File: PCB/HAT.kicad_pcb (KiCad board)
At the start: 2 copper layers, 104 parts, among them J1 Conn_01x02_Pin, J10 Conn_01x24_Socket, J11 Conn_01x24_Pin, J12 Conn_01x02_Pin, J13 Conn_01x02_Pin, J14 Conn_01x02_Pin, J15 Conn_01x02_Pin, J2 Conn_01x02_Pin, J3 Conn_01x01_Pin, J4 Conn_01x02_Pin, J5 Conn_01x10_Pin, J6 MICROXNJ, J7 Conn_01x01_Pin, J8 Conn_01x24_Pin, J9 Conn_01x24_Socket, Q1 AO3401A, Q2 LBSS84LT1G, Q3 LBSS84LT1G, Q4 BSS138, Q5 BSS138, Q6 BSS138, Q7 BSS138, Q8 LM317AG-TN3-R, U1 TP4056, U2 XC6206P, U3 OP07, U4 VL6180, U5 LM317AG, U6 CAT24C256, U7 CH340C, Y1 C252310

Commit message: PCB_Design_1
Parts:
- removed U5: LM317AG, JLC_Misc:TO-252-2_L6.5-W6.1-P4.58-LS10.0-TL
- J11, J8: footprint Connector_PinSocket_2.54mm:PinSocket_1x24_P2.54mm_Vertical -> Connector_PinHeader_2.54mm:PinHeader_1x24_P2.54mm_Vertical
- J12, J13, J14, J15: footprint Connector_PinSocket_2.54mm:PinSocket_1x02_P2.54mm_Vertical -> Connector_PinHeader_2.54mm:PinHeader_1x02_P2.54mm_Vertical
- moved R16 87.1 mm to (180.9, 52.9), turned to 90 degrees
- moved R18 85.6 mm to (180.0, 145.0)
- moved R15 83.6 mm to (177.9, 52.9), turned to 90 degrees
- moved R14 80.2 mm to (175.0, 52.9), turned to 90 degrees
- moved U4 79.0 mm to (203.1, 73.0)
- moved R19 77.7 mm to (190.1, 123.2)
- moved R20 77.7 mm to (190.1, 126.1)
- moved R21 77.7 mm to (190.1, 129.1)
- moved R22 77.7 mm to (190.1, 132.0)
- moved R23 77.7 mm to (190.1, 134.9)
- moved R24 77.7 mm to (190.1, 137.9)
- moved R25 77.7 mm to (190.1, 140.8)
- moved U3 75.8 mm to (172.6, 46.0), turned to 90 degrees
- moved D3 72.7 mm to (182.0, 47.0), turned to -90 degrees
- moved R11 70.8 mm to (158.0, 50.0)
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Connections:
- J8 pad 13: /MicroController_Interfacing/USB 5V -> Net-(J8-Pin_13)
- J9 pad 13: /MicroController_Interfacing/USB 5V -> Net-(J8-Pin_13)

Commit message: sensor layout pcb
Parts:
- moved R51 124.5 mm to (96.9, 110.0), turned to 180 degrees
- moved R50 122.5 mm to (96.6, 95.3), turned to 180 degrees
- moved R49 122.0 mm to (100.4, 113.9), turned to 90 degrees
- moved R48 120.1 mm to (100.1, 99.2), turned to 90 degrees
- moved J15 116.9 mm to (103.2, 104.8), turned to -90 degrees
- moved J14 112.3 mm to (102.8, 90.1), turned to -90 degrees
- moved R47 111.1 mm to (105.8, 114.0), turned to 90 degrees
- moved R45 110.4 mm to (106.7, 109.0), turned to 180 degrees
- moved R46 109.6 mm to (105.5, 99.3), turned to 90 degrees
- moved R44 108.8 mm to (106.4, 94.3), turned to 180 degrees
- moved U6 104.0 mm to (203.1, 121.7)
- moved R31 103.7 mm to (207.1, 79.2)
- moved R32 103.7 mm to (207.1, 82.2)
- moved R33 103.7 mm to (207.1, 85.2)
- moved R34 103.7 mm to (207.1, 88.1)
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
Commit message: Modified PCB
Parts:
- J7: value Conn_01x01_Pin -> GND
- moved J6 117.8 mm to (188.1, 68.8), turned to 90 degrees
- moved C12 101.9 mm to (169.5, 63.7), turned to 180 degrees
- moved U7 93.4 mm to (172.7, 69.1), turned to 90 degrees
- moved C15 79.0 mm to (162.8, 72.2), turned to -90 degrees
- moved J7 78.5 mm to (165.1, 57.3)
- moved U6 71.3 mm to (149.8, 74.3), turned to 90 degrees
- moved C10 65.3 mm to (136.4, 72.4), turned to 90 degrees
- moved C13 64.5 mm to (159.8, 75.7)
- moved C14 62.6 mm to (162.8, 75.6)
- moved R28 61.1 mm to (143.6, 69.5), turned to 90 degrees
- moved R26 59.0 mm to (143.9, 74.0), turned to 90 degrees
- moved R30 57.2 mm to (149.7, 69.3), turned to -90 degrees
- moved R27 56.9 mm to (147.2, 69.4), turned to 90 degrees
- moved C16 55.4 mm to (159.8, 72.2), turned to -90 degrees
- moved R29 52.8 mm to (153.3, 69.3), turned to -90 degrees
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
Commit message: PCB_Design_1
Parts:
- moved R5 59.1 mm to (94.0, 43.1), turned to -90 degrees
- moved R1 48.4 mm to (176.1, 57.0), turned to 180 degrees
- moved C4 46.9 mm to (100.0, 54.3)
- moved R6 46.8 mm to (106.0, 55.0), turned to 90 degrees
- moved C2 45.2 mm to (177.5, 48.0), turned to 180 degrees
- moved J1 43.9 mm to (171.0, 56.0)
- moved Q3 43.6 mm to (161.0, 56.2), turned to -90 degrees
- moved R17 42.6 mm to (165.1, 57.0), turned to 180 degrees
- moved LED1 41.6 mm to (115.2, 45.0), turned to 0 degrees
- moved D1 39.8 mm to (127.0, 52.0), turned to 180 degrees
- moved U2 39.2 mm to (176.0, 52.0), turned to 0 degrees
- moved LED2 38.8 mm to (115.1, 48.0), turned to 180 degrees
- moved Q1 38.8 mm to (127.0, 56.0), turned to 0 degrees
- moved R4 38.7 mm to (108.1, 48.0)
- moved U1 38.7 mm to (100.6, 44.8)
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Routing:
- net /Power Module/V_BAT+: track 0.00 -> 253.0 mm, vias 0 -> 2
- net /MicroController_Interfacing/3V3: track 0.00 -> 220.9 mm
- net /MicroController_Interfacing/A0: track 0.00 -> 123.0 mm, vias 0 -> 1
- net /MicroController_Interfacing/USB 5V: track 0.00 -> 118.3 mm, vias 0 -> 1
- net /MicroController_Interfacing/GPIO 0: track 0.00 -> 104.1 mm, vias 0 -> 1
- net /Sensor Module/Logic Level Shifting/2V8: track 0.00 -> 97.1 mm, vias 0 -> 5
- net /MicroController_Interfacing/GPIO 1: track 0.00 -> 88.6 mm, vias 0 -> 3
- net USART_TX: track 0.00 -> 82.7 mm, vias 0 -> 1
- net USART_RX: track 0.00 -> 80.7 mm, vias 0 -> 1
- net /Power Module/UVLO_3V3: track 0.00 -> 69.8 mm
- net /MicroController_Interfacing/DigitalSensorSDA: track 0.00 -> 69.7 mm
- net /Sensor Module/Logic Level Shifting/A1: track 0.00 -> 65.0 mm, vias 0 -> 1
- net Net-(D1-A): track 0.00 -> 57.0 mm
- net /MicroController_Interfacing/DigitalSensorSCL: track 0.00 -> 56.0 mm
- net /Power Module/CHRG_OUT: track 0.00 -> 48.9 mm
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- added copper zone on F.Cu, net GND

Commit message: DRCs done
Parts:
- J7: value GND -> Conn_01x01_Pin
- moved LED2 0.11 mm to (114.9, 48.0)
- moved Q2 0.10 mm to (141.1, 56.1)
- moved Q3 0.09 mm to (160.9, 56.1)
- moved C15 0.05 mm to (162.8, 72.2)
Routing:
- net GND: track 9.05 -> 213.0 mm, vias 0 -> 12
- net Net-(D1-A): track 57.0 -> 71.3 mm
- net Net-(J4-Pin_2): track 0.00 -> 7.62 mm
- net unconnected-(J6-Shield-Pad6): track 11.9 -> 13.5 mm
- net EEPROMSCL: track 17.2 -> 17.0 mm, vias 1 -> 2
- net /Sensor Module/Logic Level Shifting/2V8: vias 5 -> 4
- net /Power Module/V_BAT+: vias 2 -> 3
- added copper zone on B.Cu, net GND
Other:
- board outline added: 99.4 x 99 mm

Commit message: updated Gerbers!
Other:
- board text added: "EEE3088F GROUP 3"
- board text added: "Michael Awe AWXMIC001 Simon Carthew CRTSIM008 Adrian McIntosh MCNADR001"

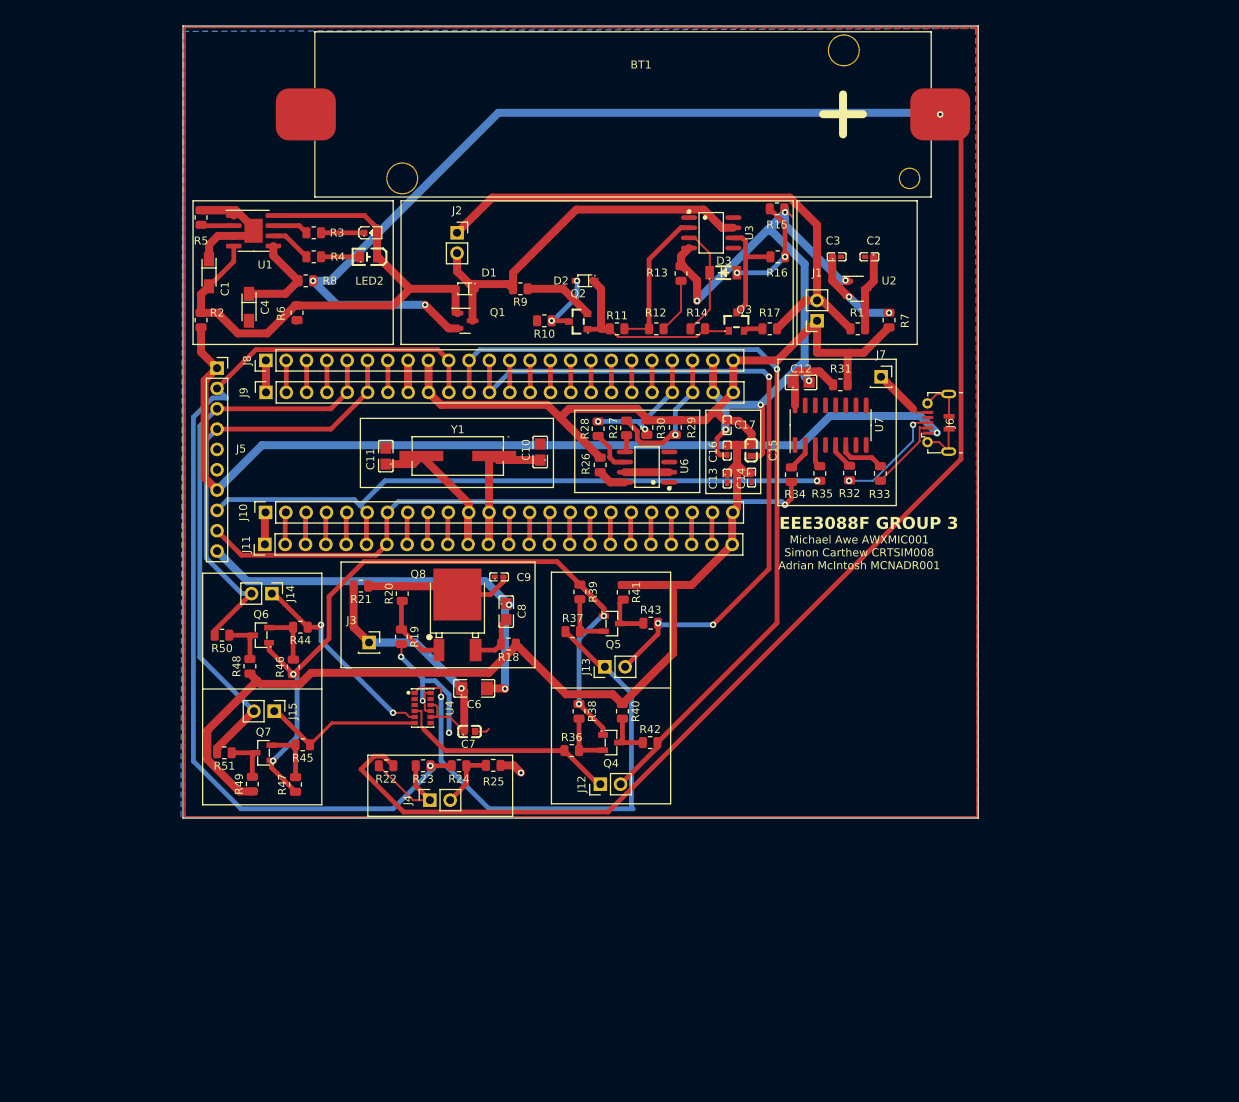
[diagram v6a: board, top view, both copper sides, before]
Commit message: Fixed via issues on PCB
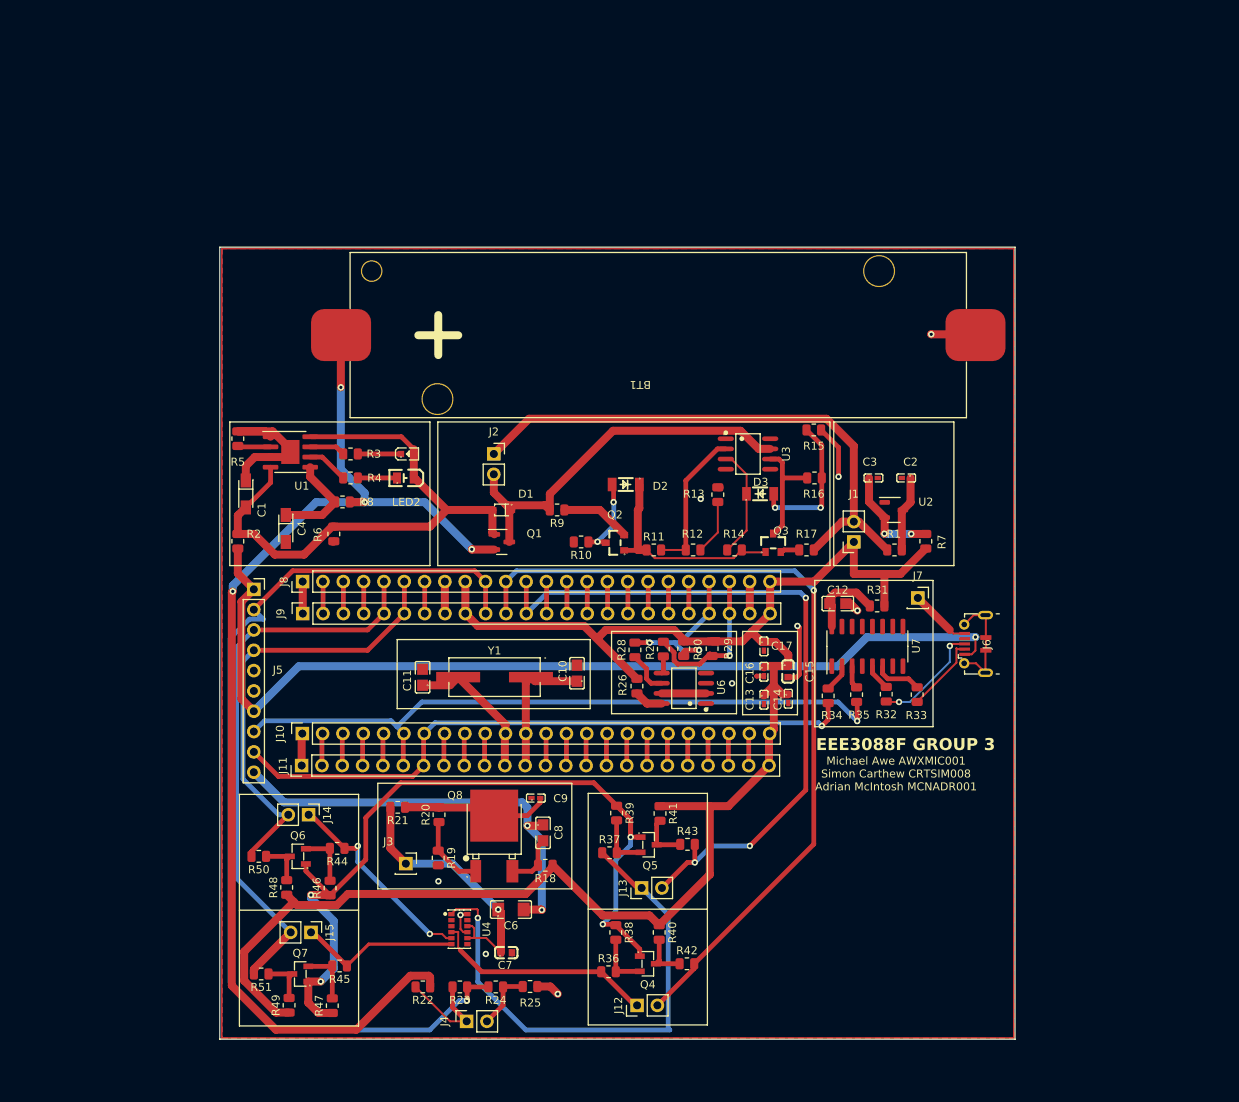
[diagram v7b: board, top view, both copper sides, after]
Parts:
- D2: value D_Schottky -> D_Zener; footprint JLC_Diodes:SOD-323_L1.8-W1.3-LS2.5-RD -> JLC_Diodes:LL-34_L3.5-W1.5-RD
- moved C13 28.0 mm to (164.4, 103.4)
- moved C14 28.0 mm to (167.4, 103.2)
- moved J12 28.0 mm to (148.5, 141.6)
- moved J13 28.0 mm to (149.1, 126.9)
- moved R10 28.0 mm to (141.5, 83.6)
- moved R12 28.0 mm to (155.5, 84.6)
- moved R26 28.0 mm to (148.5, 101.7)
- moved R29 28.0 mm to (157.9, 97.0)
- moved R31 28.0 mm to (178.5, 91.6)
- moved R39 28.0 mm to (145.9, 117.5)
- moved R9 28.0 mm to (138.5, 79.6)
- moved U3 28.0 mm to (162.4, 72.6)
- moved U6 28.0 mm to (154.4, 101.9)
- moved C1 28.0 mm to (99.6, 77.6)
- moved C15 28.0 mm to (167.4, 99.8)
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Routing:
- net /Power Module/V_BAT+: track 253.0 -> 144.7 mm, vias 3 -> 4
- net GND: track 213.0 -> 126.1 mm
- net /Sensor Module/Logic Level Shifting/2V8: track 97.1 -> 103.6 mm
- net Net-(D3-A): track 13.6 -> 18.1 mm
- net EEPROMSCL: track 17.0 -> 20.8 mm
- net USART_TX: track 82.7 -> 86.2 mm
- net Net-(D2-K): track 25.2 -> 27.0 mm
- net Net-(D2-A): track 8.77 -> 10.3 mm
- net /MicroController_Interfacing/USB 5V: track 118.3 -> 119.7 mm
- net Net-(U2-VO): track 11.6 -> 13.0 mm
- net EEPROMSDA: track 18.7 -> 19.9 mm
- net /MicroController_Interfacing/GPIO 1: track 88.6 -> 89.7 mm

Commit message: updated BOM
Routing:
- net GND: track 126.1 -> 120.5 mm
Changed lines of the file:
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@@
   (segment (start 171.5089 69.6449) (end 173.6852 71.8212) (width 0.6) (layer "F.Cu") (net 2))
   (segment (start 137.6664 139.2149) (end 138.5964 140.1449) (width 1) (layer "F.Cu") (net 2))
+  (segment (start 188.0416 95.0901) (end 189.4492 95.0901) (width 0.4) (layer "F.Cu") (net 2))
   (segment (start 190.8358 57.6921) (end 185.2763 57.6921) (width 1) (layer "F.Cu") (net 2))
-  (segment (start 189.4492 95.0901) (end 188.0416 95.0901) (width 0.25) (layer "F.Cu") (net 2))
   (segment (start 173.6852 71.8212) (end 173.6852 75.4888) (width 0.6) (layer "F.Cu") (net 2))
   (segment (start 136.546527 129.595027) (end 136.5964 129.6449) (width 1) (layer "F.Cu") (net 2))
@@
   (segment (start 126.498564 130.168436) (end 126.428745 130.238255) (width 0.4) (layer "F.Cu") (net 2))
   (segment (start 126.428745 130.269394) (end 126.428745 132.040849) (width 0.25) (layer "F.Cu") (net 2))
-  (segment (start 188.0416 95.0901) (end 187.5964 94.6449) (width 0.25) (layer "F.Cu") (net 2))
   (segment (start 136.038144 139.2149) (end 137.6664 139.2149) (width 1) (layer "F.Cu") (net 2))
   (segment (start 132.8964 134.995027) (end 132.8964 135.3449) (width 0.25) (layer "F.Cu") (net 2))
@@
   (segment (start 175.1681 91.3481) (end 176.0474 92.2274) (width 1) (layer "F.Cu") (net 2))
   (segment (start 102.9464 69.8199) (end 105.1664 72.0399) (width 1) (layer "F.Cu") (net 2))
-  (segment (start 151.578568 102.574897) (end 157.1234 102.574897) (width 1) (layer "F.Cu") (net 2))
   (segment (start 134.7968 119.1103) (end 136.6435 119.1103) (width 1) (layer "F.Cu") (net 2))
   (segment (start 99.5964 74.1449) (end 99.5964 75.958591) (width 1) (layer "F.Cu") (net 2))
@@
   (segment (start 158.5964 76.8199) (end 158.827403 76.8199) (width 1) (layer "F.Cu") (net 2))
   (segment (start 126.428745 132.040849) (end 126.806269 132.418373) (width 0.25) (layer "F.Cu") (net 2))
+  (segment (start 187.5964 94.6449) (end 188.0416 95.0901) (width 0.4) (layer "F.Cu") (net 2))
   (segment (start 174.5964 91.3481) (end 175.1681 91.3481) (width 1) (layer "F.Cu") (net 2))
   (segment (start 100.7114 73.0299) (end 99.5964 74.1449) (width 1) (layer "F.Cu") (net 2))
